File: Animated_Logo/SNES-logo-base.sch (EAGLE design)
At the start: 21 parts, among them IC1 TINY10S, Q1 BC848ALT1SMD, Q2 BC848ALT1SMD, Q3 BC848ALT1SMD, Q4 BC848ALT1SMD

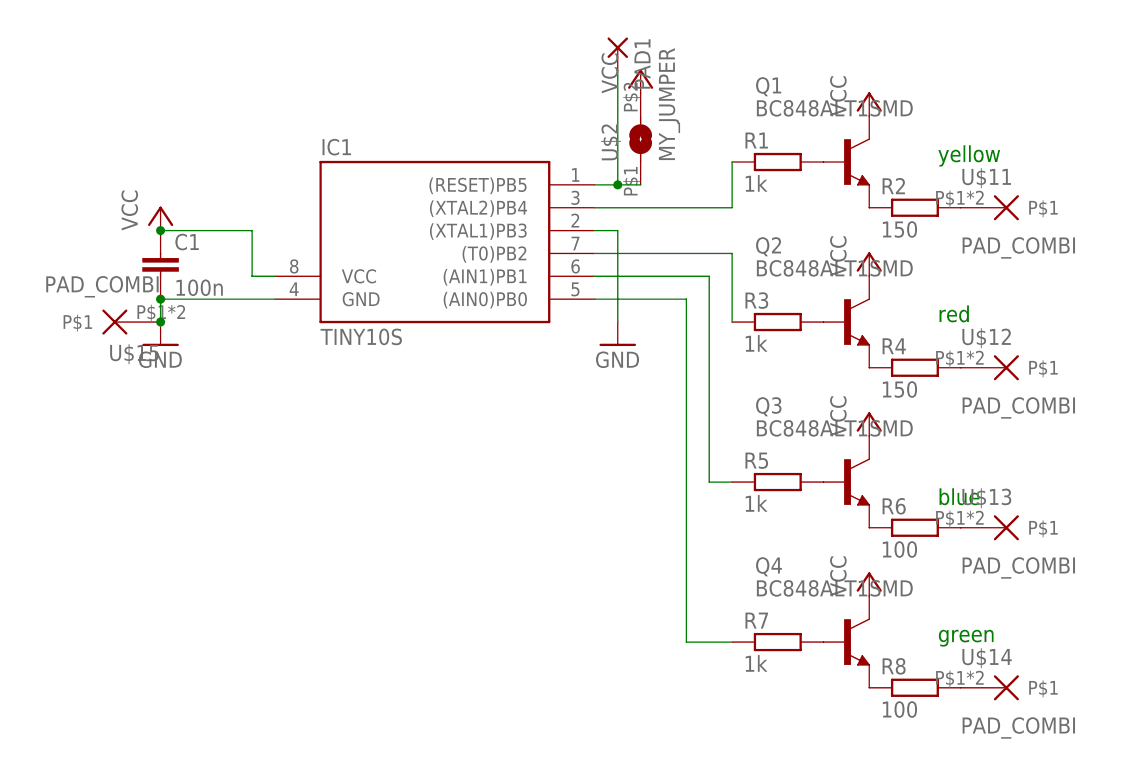
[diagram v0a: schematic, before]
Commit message: Minor updates for the Logo-PCBs: - move resistors for LEDs to the LED PCB - LEDs can be either in 0805 or P-LCC-2 package
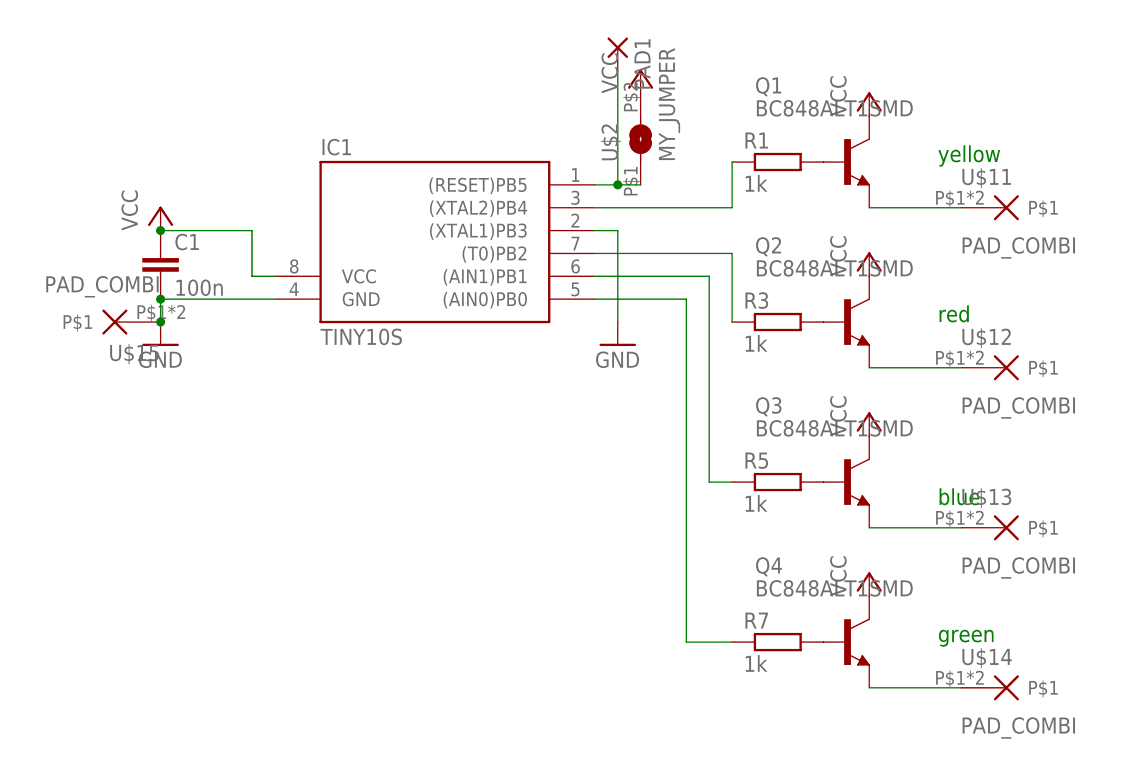
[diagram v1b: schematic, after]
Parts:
- removed R2, R4: 150, snes_div:R0805
- removed R6, R8: 100, snes_div:R0805
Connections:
- removed net N$10: Q3.E, R6.1
- removed net N$11: Q4.E, R8.1
- removed net N$16: R2.2, U$11.P$1
- removed net N$17: R4.2, U$12.P$1
- removed net N$18: R6.2, U$13.P$1
- removed net N$19: R8.2, U$14.P$1
- new net N$1: Q2.E, U$12.P$1
- new net N$3: Q3.E, U$13.P$1
- net N$8: now also Q4.E, U$14.P$1; no longer Q1.E, R2.1
- net N$9: now also Q1.E, U$11.P$1; no longer Q2.E, R4.1
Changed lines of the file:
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@@
 <part name="R5" library="snes_div" deviceset="R0805" device="" value="1k"/>
 <part name="R7" library="snes_div" deviceset="R0805" device="" value="1k"/>
-<part name="R2" library="snes_div" deviceset="R0805" device="" value="150"/>
-<part name="R4" library="snes_div" deviceset="R0805" device="" value="150"/>
-<part name="R6" library="snes_div" deviceset="R0805" device="" value="100"/>
-<part name="R8" library="snes_div" deviceset="R0805" device="" value="100"/>
 <part name="U$11" library="MS_Mod" deviceset="PAD_COMBI" device=""/>
 <part name="U$12" library="MS_Mod" deviceset="PAD_COMBI" device=""/>
@@
 <instance part="R5" gate="G$1" x="81.28" y="30.48"/>
 <instance part="R7" gate="G$1" x="81.28" y="12.7"/>
-<instance part="R2" gate="G$1" x="96.52" y="60.96"/>
-<instance part="R4" gate="G$1" x="96.52" y="43.18"/>
-<instance part="R6" gate="G$1" x="96.52" y="25.4"/>
-<instance part="R8" gate="G$1" x="96.52" y="7.62"/>
 <instance part="U$11" gate="G$1" x="106.68" y="60.96"/>
 <instance part="U$12" gate="G$1" x="106.68" y="43.18"/>
@@
 </segment>
 </net>
-<net name="N$8" class="0">
-<segment>
-<pinref part="Q1" gate="G$1" pin="E"/>
-<pinref part="R2" gate="G$1" pin="1"/>
-</segment>
-</net>
-<net name="N$9" class="0">
-<segment>
-<pinref part="Q2" gate="G$1" pin="E"/>
-<pinref part="R4" gate="G$1" pin="1"/>
-</segment>
-</net>
-<net name="N$10" class="0">
-<segment>
-<pinref part="Q3" gate="G$1" pin="E"/>
-<pinref part="R6" gate="G$1" pin="1"/>
-</segment>
-</net>
-<net name="N$11" class="0">
-<segment>
-<pinref part="Q4" gate="G$1" pin="E"/>
-<pinref part="R8" gate="G$1" pin="1"/>
-</segment>
-</net>
 <net name="N$12" class="0">
 <segment>
@@
 </segment>
 </net>
-<net name="N$16" class="0">
-<segment>
-<pinref part="R2" gate="G$1" pin="2"/>
-<pinref part="U$11" gate="G$1" pin="P$1"/>
-</segment>
-</net>
-<net name="N$17" class="0">
-<segment>
-<pinref part="R4" gate="G$1" pin="2"/>
-<pinref part="U$12" gate="G$1" pin="P$1"/>
-</segment>
-</net>
-<net name="N$18" class="0">
-<segment>
-<pinref part="R6" gate="G$1" pin="2"/>
-<pinref part="U$13" gate="G$1" pin="P$1"/>
-</segment>
-</net>
-<net name="N$19" class="0">
-<segment>
-<pinref part="R8" gate="G$1" pin="2"/>
-<pinref part="U$14" gate="G$1" pin="P$1"/>
-</segment>
-</net>
 <net name="N$2" class="0">
 <segment>
@@
 </segment>
 </net>
+<net name="N$1" class="0">
+<segment>
+<pinref part="U$12" gate="G$1" pin="P$1"/>
+<pinref part="Q2" gate="G$1" pin="E"/>
+<wire x1="101.6" y1="43.18" x2="91.44" y2="43.18" width="0.1524" layer="91"/>
+</segment>
+</net>
+<net name="N$3" class="0">
+<segment>
+<pinref part="U$13" gate="G$1" pin="P$1"/>
+<pinref part="Q3" gate="G$1" pin="E"/>
+<wire x1="101.6" y1="25.4" x2="91.44" y2="25.4" width="0.1524" layer="91"/>
+</segment>
+</net>
+<net name="N$8" class="0">
+<segment>
+<pinref part="U$14" gate="G$1" pin="P$1"/>
+<pinref part="Q4" gate="G$1" pin="E"/>
+<wire x1="101.6" y1="7.62" x2="91.44" y2="7.62" width="0.1524" layer="91"/>
+</segment>
+</net>
+<net name="N$9" class="0">
+<segment>
+<pinref part="U$11" gate="G$1" pin="P$1"/>
+<pinref part="Q1" gate="G$1" pin="E"/>
+<wire x1="101.6" y1="60.96" x2="91.44" y2="60.96" width="0.1524" layer="91"/>
+</segment>
+</net>
